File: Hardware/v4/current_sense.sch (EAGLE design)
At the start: 40 parts, among them J1 SCREW-TERMINAL_2_0.100, J2 SCREW-TERMINAL_2_0.100, J3 SCREW-TERMINAL_2_0.100, J4 SCREW-TERMINAL_2_0.100, U1 MAX9923H, U2 LP3985

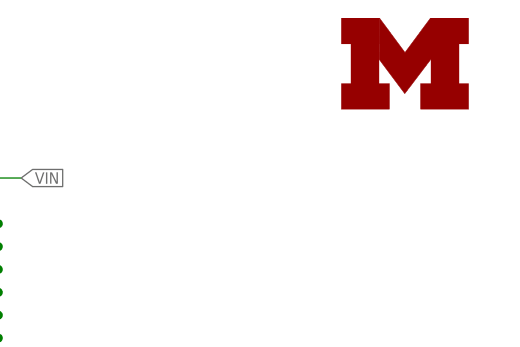
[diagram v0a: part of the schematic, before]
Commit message: Fix resistance issues, all doc on silk now
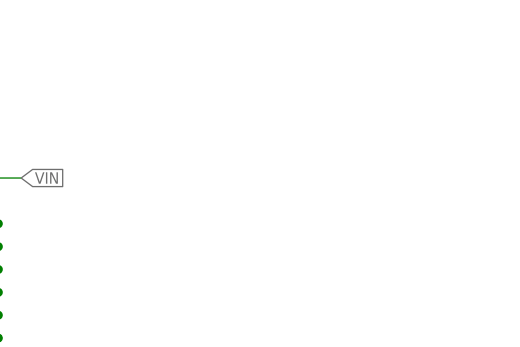
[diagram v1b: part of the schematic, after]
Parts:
- removed LOGO2: UMICH_SOLID_MEDIUM, logos:UMICH_SOLID_MEDIUM
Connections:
- net N$1 renamed RS-_100UA
- net N$2 renamed RS-_1MA
- net N$3 renamed RS-_10MA
- net N$4 renamed RS-_30MA
- net N$5 renamed RS-_60MA
- net N$6 renamed RS-_100MA
- net N$7 renamed SENSE_FB
- net N$8 renamed LDO_BYPASS
- net N$9 renamed RS-_300MA
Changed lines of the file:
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@@
 <?xml version="1.0" encoding="utf-8"?>
 <!DOCTYPE eagle SYSTEM "eagle.dtd">
-<eagle version="6.5.0">
+<eagle version="8.7.1">
 <drawing>
 <settings>
 <setting alwaysvectorfont="no"/>
+<setting keepoldvectorfont="yes"/>
 <setting verticaltext="up"/>
 </settings>
-<grid distance="0.1" unitdist="inch" unit="inch" style="lines" multiple="1" display="no" altdistance="0.01" altunitdist="inch" altunit="inch"/>
+<grid distance="0.1" unitdist="inch" unit="inch" style="lines" multiple="1" display="yes" altdistance="0.05" altunitdist="inch" altunit="inch"/>
 <layers>
 <layer number="1" name="Top" color="4" fill="1" visible="no" active="no"/>
@@
 <attribute name="DIGIKEY" value="CKN10705-ND"/>
 </part>
-<part name="LOGO2" library="logos" deviceset="UMICH_SOLID" device="_MEDIUM"/>
 </parts>
 <sheets>
@@
 <attribute name="DIGIKEY" x="170.18" y="152.4" size="1.27" layer="96" align="center-left" display="off"/>
 </instance>
-<instance part="LOGO2" gate="G$1" x="231.14" y="172.72"/>
 </instances>
 <busses>
@@
 </segment>
 </net>
-<net name="N$1" class="0">
+<net name="RS-_100UA" class="0">
 <segment>
 <pinref part="R7" gate="G$1" pin="1"/>
@@
 </segment>
 </net>
-<net name="N$2" class="0">
+<net name="RS-_1MA" class="0">
 <segment>
 <pinref part="R6" gate="G$1" pin="1"/>
@@
 </segment>
 </net>
-<net name="N$3" class="0">
+<net name="RS-_10MA" class="0">
 <segment>
 <pinref part="R5" gate="G$1" pin="1"/>
@@
 </segment>
 </net>
-<net name="N$4" class="0">
+<net name="RS-_30MA" class="0">
 <segment>
 <pinref part="R4" gate="G$1" pin="1"/>
@@
 </segment>
 </net>
-<net name="N$5" class="0">
+<net name="RS-_60MA" class="0">
 <segment>
 <pinref part="R3" gate="G$1" pin="1"/>
@@
 </segment>
 </net>
-<net name="N$6" class="0">
+<net name="RS-_100MA" class="0">
 <segment>
 <pinref part="R2" gate="G$1" pin="1"/>
@@
 </segment>
 </net>
-<net name="N$7" class="0">
+<net name="SENSE_FB" class="0">
 <segment>
 <pinref part="R9" gate="G$1" pin="1"/>
@@
 </segment>
 </net>
-<net name="N$8" class="0">
+<net name="LDO_BYPASS" class="0">
 <segment>
 <pinref part="C1" gate="G$1" pin="1"/>
@@
 </segment>
 </net>
-<net name="N$9" class="0">
+<net name="RS-_300MA" class="0">
 <segment>
 <pinref part="S1" gate="G$1" pin="G"/>
